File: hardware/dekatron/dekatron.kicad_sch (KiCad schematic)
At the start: 0 parts

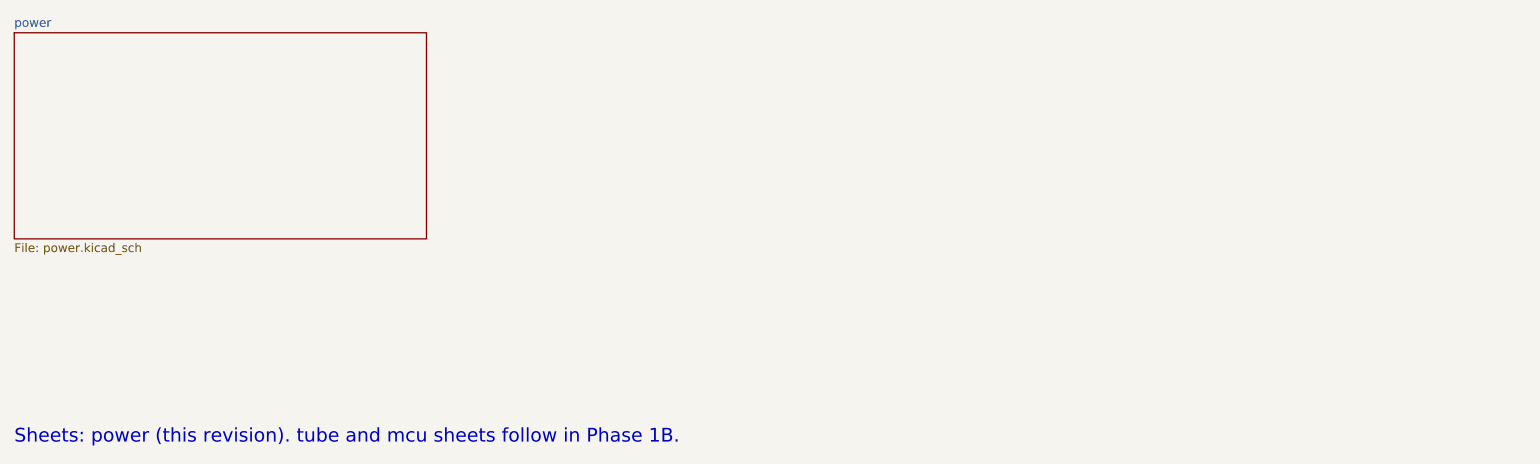
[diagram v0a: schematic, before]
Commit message: Tube sheet schematic; kit 15 uH buck inductor
tube.kicad_sch: G+/RTN zener regulator from V_B_BIAS (RTN 51 V sinks the
tube current and holds with zero tube current; G+ = 90 V), MMBTA42 guide
drivers, MMBTA92 index level shifter, 3 x 220k anode string, cathode
links LK6-LK14 and soldered harness landings. Net classes extended to
ANODE (HV) and the bias nets. BOM now covers both sheets (bom.csv).
Buck inductor from the user's kit: 15 uH, 1.31 A, 4 mm pitch.

Co-Authored-By: Claude Opus 5.5 <noreply@anthropic.com>
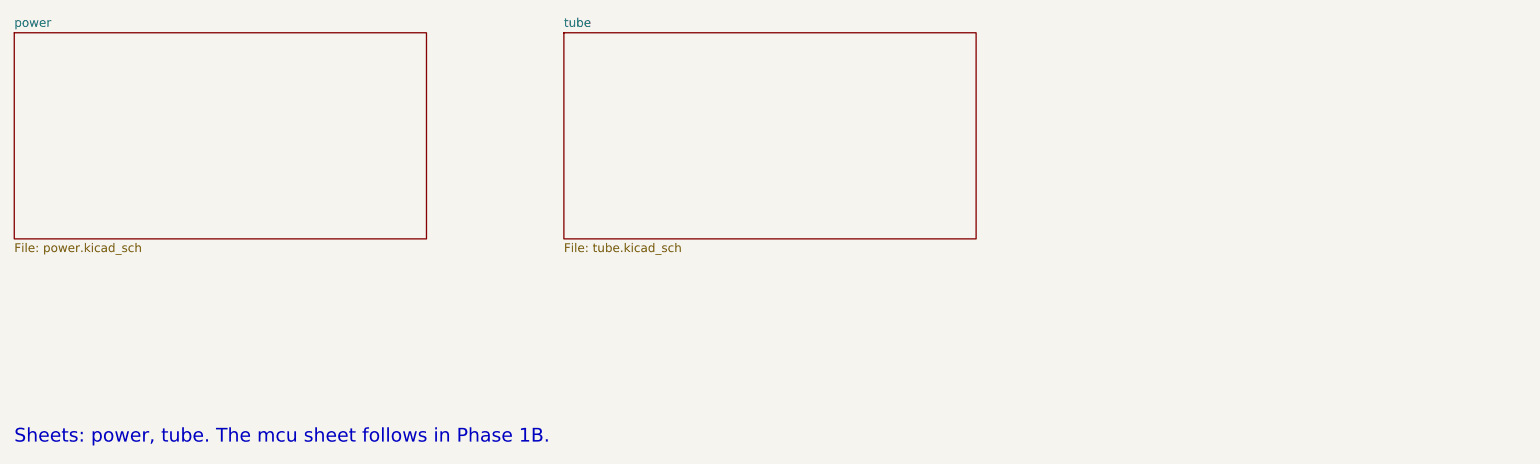
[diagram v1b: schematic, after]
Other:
- added sheet tube (tube.kicad_sch)
- note added: "Sheets: power, tube. The mcu sheet follows in Phase 1B."
- note removed: "Sheets: power (this revision). tube and mcu sheets follow in Phase 1B."
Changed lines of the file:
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@@
 	  (instances (project "dekatron" (path "/b14ce2c4-03a1-5284-8a98-bc460407f799" (page "2"))))
 	)
-	(text "Sheets: power (this revision). tube and mcu sheets follow in Phase 1B." (exclude_from_sim no) (at 40 100 0) (effects (font (size 2 2)) (justify left bottom)))
+	(sheet (at 120 40) (size 60 30) (exclude_from_sim no) (in_bom yes) (on_board yes) (dnp no)
+	  (stroke (width 0.1524) (type solid)) (fill (color 0 0 0 0.0000))
+	  (property "Sheetname" "tube" (at 120 39.2884 0) (show_name no) (do_not_autoplace no) (effects (font (size 1.27 1.27)) (justify left bottom)))
+	  (property "Sheetfile" "tube.kicad_sch" (at 120 70.5846 0) (show_name no) (do_not_autoplace no) (effects (font (size 1.27 1.27)) (justify left top)))
+	  (instances (project "dekatron" (path "/b14ce2c4-03a1-5284-8a98-bc460407f799" (page "3"))))
+	)
+	(text "Sheets: power, tube. The mcu sheet follows in Phase 1B." (exclude_from_sim no) (at 40 100 0) (effects (font (size 2 2)) (justify left bottom)))
 	(sheet_instances (path "/" (page "1")))
 	(embedded_fonts no)

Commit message: MCU sheet schematic with RP2040-Zero symbol and castellated footprint
mcu.kicad_sch: RP2040-Zero per the Phase 1A pin map, BAT54S clamps and
reservoir capacitors on the four ADC inputs, VIN_SENSE divider, I2C
pull-ups, DISP and NIX_LV harness landings, test points. The project
footprint follows Waveshare's pinout and STEP-model geometry (2.54 mm
pitch, 15.24 mm column spacing) with pads extended for hand soldering.
ERC across all three sheets: 1 violation, the intentional LP2951 to
LM5156 VCC connection.

Co-Authored-By: Claude Opus 5.5 <noreply@anthropic.com>
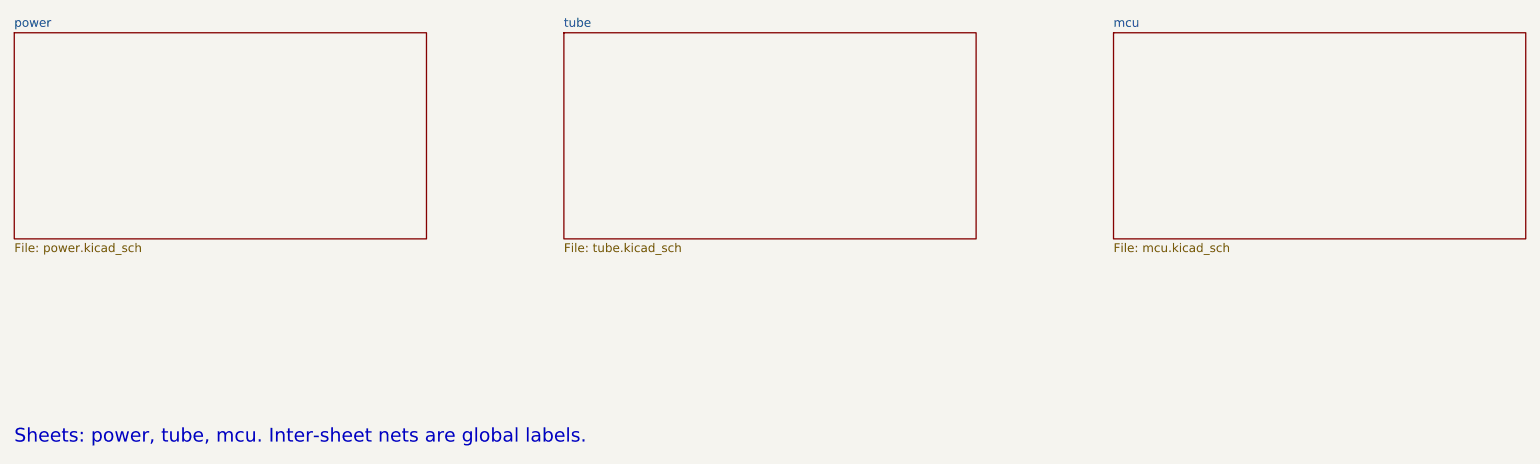
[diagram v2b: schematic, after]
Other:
- added sheet mcu (mcu.kicad_sch)
- note added: "Sheets: power, tube, mcu. Inter-sheet nets are global labels."
- note removed: "Sheets: power, tube. The mcu sheet follows in Phase 1B."
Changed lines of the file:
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@@
 	  (instances (project "dekatron" (path "/b14ce2c4-03a1-5284-8a98-bc460407f799" (page "3"))))
 	)
-	(text "Sheets: power, tube. The mcu sheet follows in Phase 1B." (exclude_from_sim no) (at 40 100 0) (effects (font (size 2 2)) (justify left bottom)))
+	(sheet (at 200 40) (size 60 30) (exclude_from_sim no) (in_bom yes) (on_board yes) (dnp no)
+	  (stroke (width 0.1524) (type solid)) (fill (color 0 0 0 0.0000))
+	  (property "Sheetname" "mcu" (at 200 39.2884 0) (show_name no) (do_not_autoplace no) (effects (font (size 1.27 1.27)) (justify left bottom)))
+	  (property "Sheetfile" "mcu.kicad_sch" (at 200 70.5846 0) (show_name no) (do_not_autoplace no) (effects (font (size 1.27 1.27)) (justify left top)))
+	  (instances (project "dekatron" (path "/b14ce2c4-03a1-5284-8a98-bc460407f799" (page "4"))))
+	)
+	(text "Sheets: power, tube, mcu. Inter-sheet nets are global labels." (exclude_from_sim no) (at 40 100 0) (effects (font (size 2 2)) (justify left bottom)))
 	(sheet_instances (path "/" (page "1")))
 	(embedded_fonts no)
